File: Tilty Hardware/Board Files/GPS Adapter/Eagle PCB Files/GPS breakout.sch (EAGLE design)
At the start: 10 parts, among them U1 XBEE-1XBEE-1_LOCK, U2 LM2931, U3 V_REG_LDOSMD

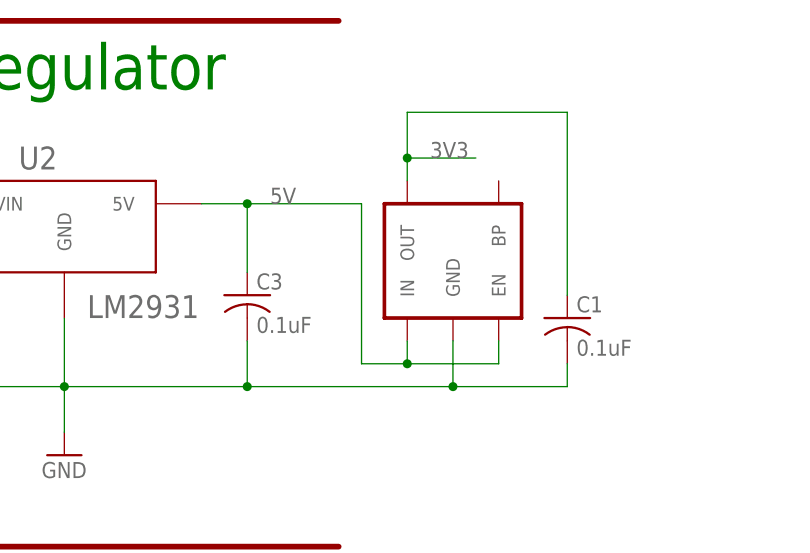
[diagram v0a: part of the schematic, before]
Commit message: Nearly finished RC Receiver add-on prototype, worked on TiltyIMU library
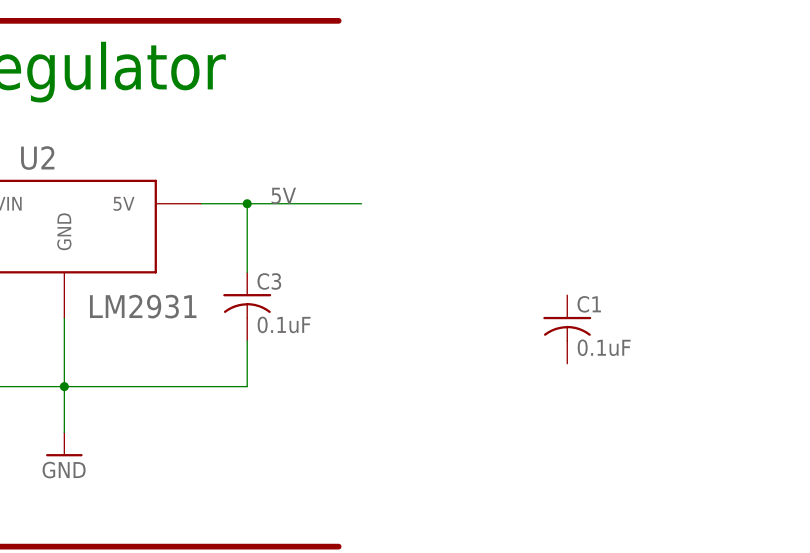
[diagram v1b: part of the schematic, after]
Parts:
- removed U3: V_REG_LDOSMD, SparkFun-PowerIC:V_REG_LDOSMD
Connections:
- net 3V3: no longer C1.1, U3.OUT
- net 5V: no longer U3.EN, U3.IN
- net GND: no longer C1.2, U3.GND
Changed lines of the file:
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@@
 <part name="GND21" library="supply1" deviceset="GND" device=""/>
 <part name="U1" library="SparkFun-RF" deviceset="XBEE-1" device="XBEE-1_LOCK"/>
-<part name="U3" library="SparkFun-PowerIC" deviceset="V_REG_LDO" device="SMD">
-<attribute name="PART#" value="TLV71333PDBVR"/>
-</part>
 <part name="C1" library="resistor" deviceset="C-US" device="C0603" value="0.1uF"/>
 </parts>
@@
 <instance part="GND21" gate="1" x="228.6" y="7.62"/>
 <instance part="U1" gate="G$1" x="71.12" y="43.18"/>
-<instance part="U3" gate="G$1" x="185.42" y="109.22" smashed="yes" rot="R90">
-<attribute name="PART#" x="185.42" y="109.22" size="1.778" layer="96" rot="R90" display="off"/>
-</instance>
 <instance part="C1" gate="G$1" x="198.12" y="101.6"/>
 </instances>
@@
 <wire x1="121.92" y1="99.06" x2="121.92" y2="93.98" width="0.1524" layer="91"/>
 <wire x1="121.92" y1="93.98" x2="142.24" y2="93.98" width="0.1524" layer="91"/>
-<pinref part="U3" gate="G$1" pin="GND"/>
-<wire x1="185.42" y1="99.06" x2="185.42" y2="93.98" width="0.1524" layer="91"/>
-<wire x1="185.42" y1="93.98" x2="162.56" y2="93.98" width="0.1524" layer="91"/>
-<junction x="162.56" y="93.98"/>
-<pinref part="C1" gate="G$1" pin="2"/>
-<wire x1="198.12" y1="96.52" x2="198.12" y2="93.98" width="0.1524" layer="91"/>
-<wire x1="198.12" y1="93.98" x2="185.42" y2="93.98" width="0.1524" layer="91"/>
-<junction x="185.42" y="93.98"/>
 </segment>
 <segment>
@@
 <wire x1="162.56" y1="106.68" x2="162.56" y2="114.3" width="0.1524" layer="91"/>
 <junction x="162.56" y="114.3"/>
-<wire x1="175.26" y1="114.3" x2="175.26" y2="96.52" width="0.1524" layer="91"/>
-<pinref part="U3" gate="G$1" pin="IN"/>
-<wire x1="175.26" y1="96.52" x2="180.34" y2="96.52" width="0.1524" layer="91"/>
-<wire x1="180.34" y1="96.52" x2="180.34" y2="99.06" width="0.1524" layer="91"/>
-<pinref part="U3" gate="G$1" pin="EN"/>
-<wire x1="180.34" y1="96.52" x2="190.5" y2="96.52" width="0.1524" layer="91"/>
-<wire x1="190.5" y1="96.52" x2="190.5" y2="99.06" width="0.1524" layer="91"/>
-<junction x="180.34" y="96.52"/>
 </segment>
 <segment>
@@
 <net name="3V3" class="3">
 <segment>
-<pinref part="U3" gate="G$1" pin="OUT"/>
-<wire x1="180.34" y1="116.84" x2="180.34" y2="119.38" width="0.1524" layer="91"/>
-<wire x1="180.34" y1="119.38" x2="187.96" y2="119.38" width="0.1524" layer="91"/>
-<label x="182.88" y="119.38" size="1.778" layer="95"/>
-<pinref part="C1" gate="G$1" pin="1"/>
-<wire x1="198.12" y1="104.14" x2="198.12" y2="124.46" width="0.1524" layer="91"/>
-<wire x1="198.12" y1="124.46" x2="180.34" y2="124.46" width="0.1524" layer="91"/>
-<wire x1="180.34" y1="124.46" x2="180.34" y2="119.38" width="0.1524" layer="91"/>
-<junction x="180.34" y="119.38"/>
-</segment>
-<segment>
 <pinref part="JP1" gate="A" pin="8"/>

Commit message: GPS breakout work, and minor Tilty Omni changes
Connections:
- removed net N$10: JP6.8
- removed net N$23: JP6.7
- net 5V: no longer JP5.8
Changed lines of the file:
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@@
 </plain>
 <instances>
-<instance part="GND10" gate="1" x="205.74" y="71.12" rot="R180"/>
+<instance part="GND10" gate="1" x="231.14" y="63.5" rot="R180"/>
 <instance part="GND12" gate="1" x="142.24" y="86.36"/>
 <instance part="U2" gate="G$1" x="142.24" y="111.76">
@@
 </segment>
 <segment>
-<pinref part="GND10" gate="1" pin="GND"/>
-<wire x1="205.74" y1="55.88" x2="203.2" y2="55.88" width="0.1524" layer="91"/>
-<wire x1="205.74" y1="55.88" x2="205.74" y2="68.58" width="0.1524" layer="91"/>
-<junction x="205.74" y="55.88"/>
-<wire x1="205.74" y1="55.88" x2="210.82" y2="55.88" width="0.1524" layer="91"/>
-<wire x1="210.82" y1="55.88" x2="210.82" y2="58.42" width="0.1524" layer="91"/>
-<pinref part="JP5" gate="A" pin="7"/>
-<wire x1="210.82" y1="58.42" x2="241.3" y2="58.42" width="0.1524" layer="91"/>
-</segment>
-<segment>
 <pinref part="JP2" gate="A" pin="1"/>
 <wire x1="149.86" y1="22.86" x2="154.94" y2="22.86" width="0.1524" layer="91"/>
@@
 <pinref part="GND21" gate="1" pin="GND"/>
 </segment>
+<segment>
+<pinref part="JP5" gate="A" pin="7"/>
+<pinref part="GND10" gate="1" pin="GND"/>
+<wire x1="241.3" y1="58.42" x2="231.14" y2="58.42" width="0.1524" layer="91"/>
+<wire x1="231.14" y1="58.42" x2="231.14" y2="60.96" width="0.1524" layer="91"/>
+</segment>
 </net>
 <net name="SCL" class="4">
 <segment>
-<wire x1="203.2" y1="38.1" x2="217.17" y2="38.1" width="0.1524" layer="91"/>
-<wire x1="217.17" y1="38.1" x2="217.17" y2="45.72" width="0.1524" layer="91"/>
 <pinref part="JP5" gate="A" pin="2"/>
-<wire x1="217.17" y1="45.72" x2="241.3" y2="45.72" width="0.1524" layer="91"/>
-<label x="203.2" y="38.1" size="1.778" layer="95"/>
+<wire x1="224.79" y1="45.72" x2="241.3" y2="45.72" width="0.1524" layer="91"/>
+<label x="226.06" y="45.72" size="1.778" layer="95"/>
 </segment>
 </net>
 <net name="SDA" class="4">
 <segment>
-<wire x1="203.2" y1="35.56" x2="218.44" y2="35.56" width="0.1524" layer="91"/>
-<label x="203.2" y="35.56" size="1.778" layer="95"/>
 <pinref part="JP5" gate="A" pin="1"/>
-<wire x1="218.44" y1="35.56" x2="218.44" y2="43.18" width="0.1524" layer="91"/>
-<wire x1="218.44" y1="43.18" x2="241.3" y2="43.18" width="0.1524" layer="91"/>
+<wire x1="226.06" y1="43.18" x2="241.3" y2="43.18" width="0.1524" layer="91"/>
+<label x="228.6" y="43.18" size="1.778" layer="95"/>
 </segment>
 </net>
@@
 </segment>
 </net>
-<net name="TEENSY_3V3" class="3">
-<segment>
-<wire x1="203.2" y1="58.42" x2="208.28" y2="58.42" width="0.1524" layer="91"/>
-<wire x1="208.28" y1="58.42" x2="208.28" y2="66.04" width="0.1524" layer="91"/>
-<wire x1="208.28" y1="66.04" x2="223.52" y2="66.04" width="0.1524" layer="91"/>
-<label x="208.28" y="66.04" size="1.778" layer="95"/>
-</segment>
-</net>
 <net name="5V" class="0">
 <segment>
@@
 <junction x="162.56" y="114.3"/>
 </segment>
-<segment>
-<pinref part="JP5" gate="A" pin="8"/>
-<wire x1="203.2" y1="60.96" x2="241.3" y2="60.96" width="0.1524" layer="91"/>
-<label x="210.82" y="60.96" size="1.778" layer="95"/>
-</segment>
 </net>
-<net name="N$23" class="0">
-<segment>
-<wire x1="203.2" y1="30.48" x2="220.98" y2="30.48" width="0.1524" layer="91"/>
-<pinref part="JP6" gate="A" pin="7"/>
-<wire x1="220.98" y1="30.48" x2="220.98" y2="35.56" width="0.1524" layer="91"/>
-<wire x1="220.98" y1="35.56" x2="233.68" y2="35.56" width="0.1524" layer="91"/>
-</segment>
-</net>
-<net name="N$10" class="0">
-<segment>
-<wire x1="203.2" y1="33.02" x2="219.71" y2="33.02" width="0.1524" layer="91"/>
-<wire x1="219.71" y1="33.02" x2="219.71" y2="38.1" width="0.1524" layer="91"/>
-<pinref part="JP6" gate="A" pin="8"/>
-<wire x1="219.71" y1="38.1" x2="233.68" y2="38.1" width="0.1524" layer="91"/>
-</segment>
-</net>
